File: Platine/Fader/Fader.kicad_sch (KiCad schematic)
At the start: 9 parts, among them J1 FaderPWR, J2 FaderSignal, J3 Motor13Out, J4 Motor4Out, J5 Conn_01x19, J6 Conn_01x19, U1 MC12, U3 MC34, U4 YAAJ_DCDC_StepDown_LM2596

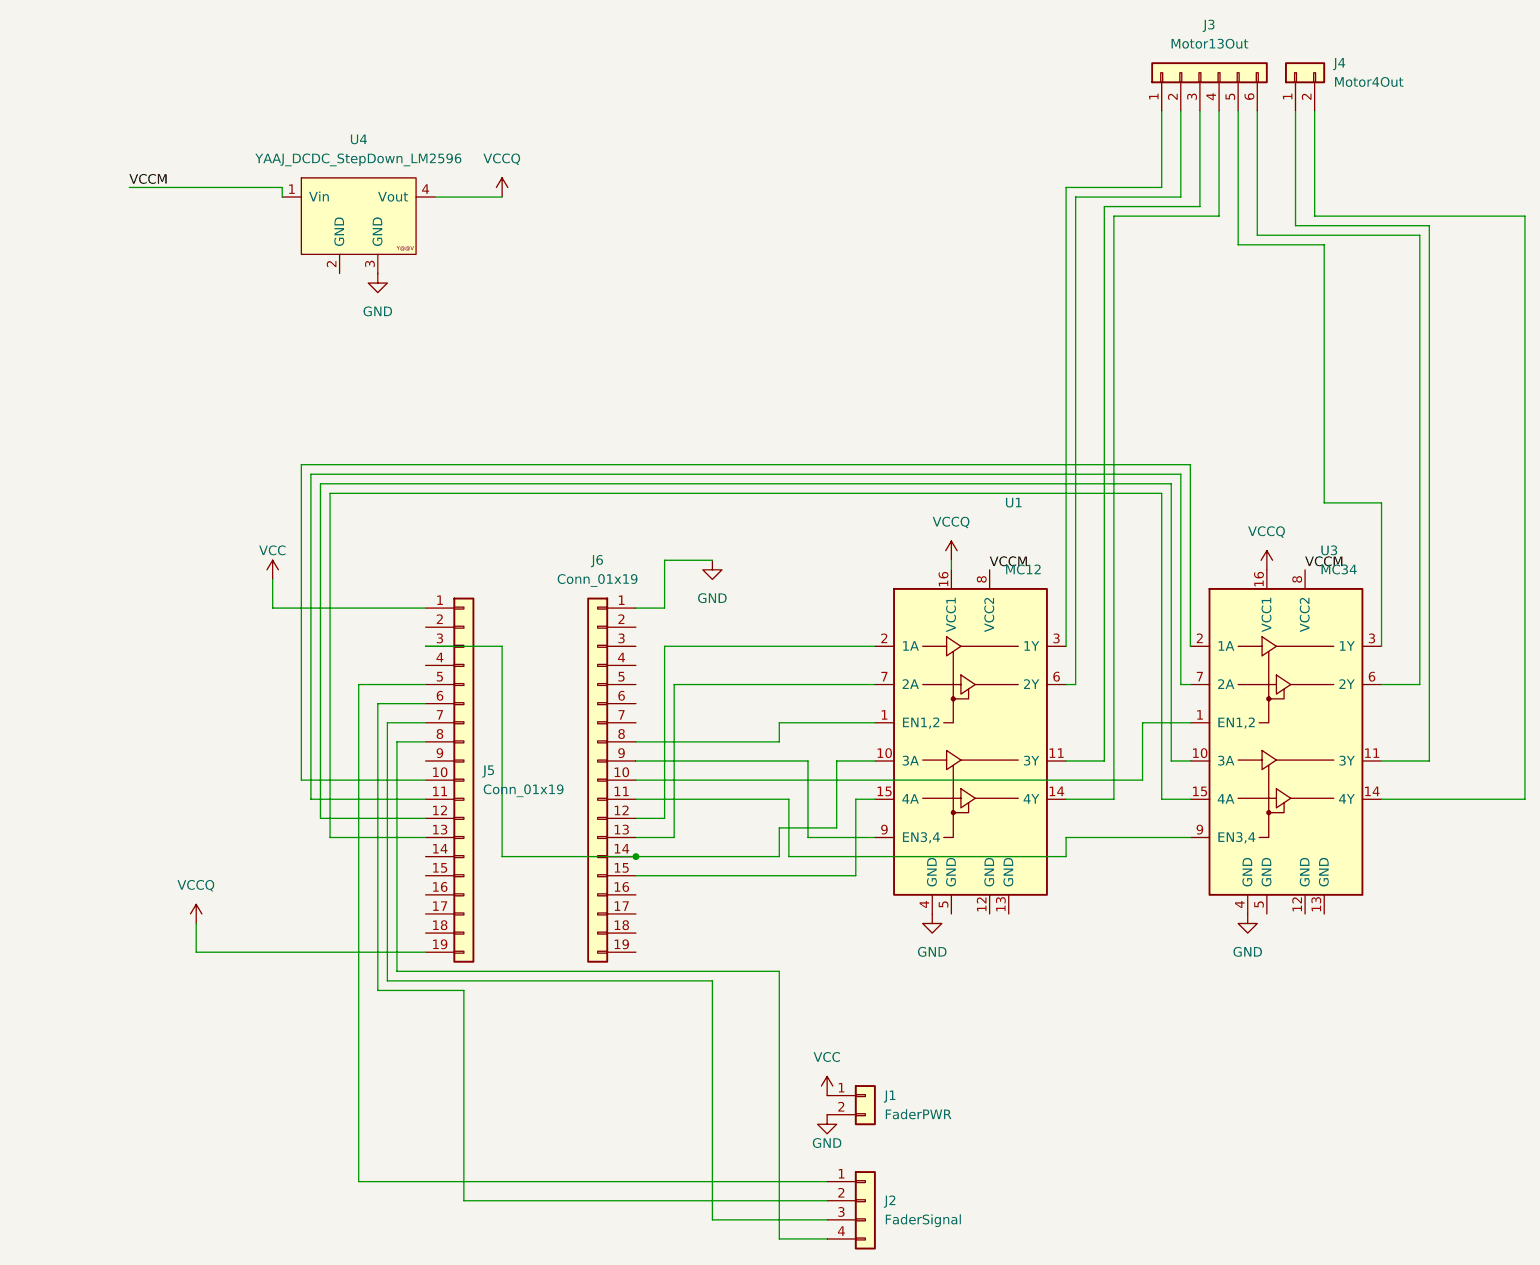
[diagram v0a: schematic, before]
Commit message: Rearranged pcb schematic. Added first traces and coorect ESP32 footprint model
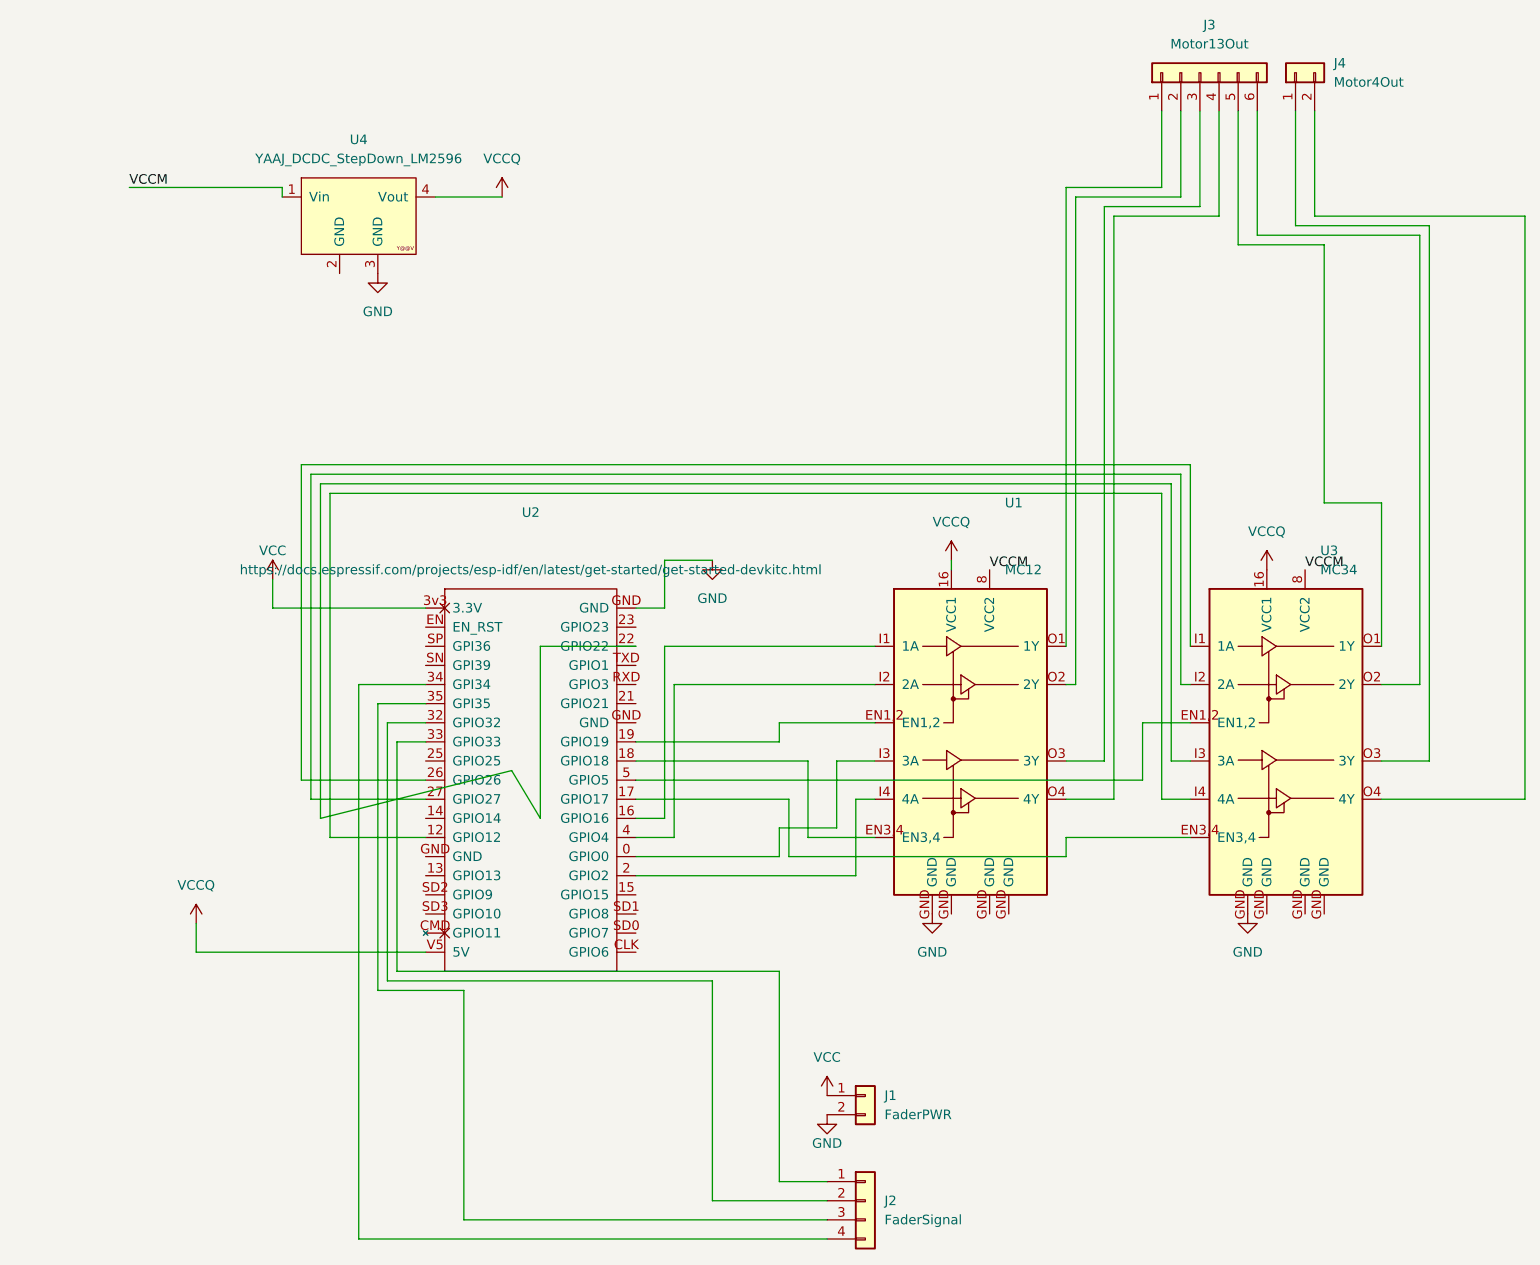
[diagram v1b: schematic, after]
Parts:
- removed J5: Conn_01x19, fp_esp32_dev4:esp32_dev_left, symbol Connector_Generic:Conn_01x19
- removed J6: Conn_01x19, fp_esp32_dev4:esp32_dev4_right, symbol Connector_Generic:Conn_01x19
- added U2: (no value), symbol New_Library:esp32_38_pins-custom_library
- U1, U3: symbol Driver_Motor:L293D -> New_Library:L293D
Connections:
- net GND: now also U1.GND, U3.GND, U2.GND; no longer U1.4 (GND), U3.4 (GND)
- net VCC: now also U2.3v3 (3.3V)
- net VCCQ: now also U2.V5 (5V)
- net at J3.1 (Pin_1): now also U1.O1 (1Y); no longer U1.3 (1Y)
- net at J3.2 (Pin_2): now also U1.O2 (2Y); no longer U1.6 (2Y)
- net at J3.3 (Pin_3): now also U1.O3 (3Y); no longer U1.11 (3Y)
- net at J3.4 (Pin_4): now also U1.O4 (4Y); no longer U1.14 (4Y)
- net at J3.5 (Pin_5): now also U3.O1 (1Y); no longer U3.3 (1Y)
- net at J3.6 (Pin_6): now also U3.O2 (2Y); no longer U3.6 (2Y)
- net at J4.1 (Pin_1): now also U3.O3 (3Y); no longer U3.11 (3Y)
- net at J4.2 (Pin_2): now also U3.O4 (4Y); no longer U3.14 (4Y)
- net at J2.1 (Pin_1): now also U2.33 (GPIO33)
- net at J2.2 (Pin_2): now also U2.32 (GPIO32)
- net at J2.3 (Pin_3): now also U2.35 (GPI35)
- net at J2.4 (Pin_4): now also U2.34 (GPI34)
- new net: U1.I3 (3A), U2.0 (GPIO0)
- new net: U2.12 (GPIO12), U3.I4 (4A)
- new net: U1.I1 (1A), U2.16 (GPIO16)
- new net: U2.17 (GPIO17), U3.EN3,4
- new net: U1.EN3,4, U2.18 (GPIO18)
- new net: U1.EN1,2, U2.19 (GPIO19)
- new net: U1.I4 (4A), U2.2 (GPIO2)
- new net: U2.22 (GPIO22), U3.I3 (3A)
- new net: U2.26 (GPIO26), U3.I1 (1A)
- new net: U2.27 (GPIO27), U3.I2 (2A)
- new net: U1.I2 (2A), U2.4 (GPIO4)
- new net: U2.5 (GPIO5), U3.EN1,2
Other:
- moved on the sheet: U1, U3

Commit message: Connect Slider Touch Pins to ESP32 touch sensitive pins
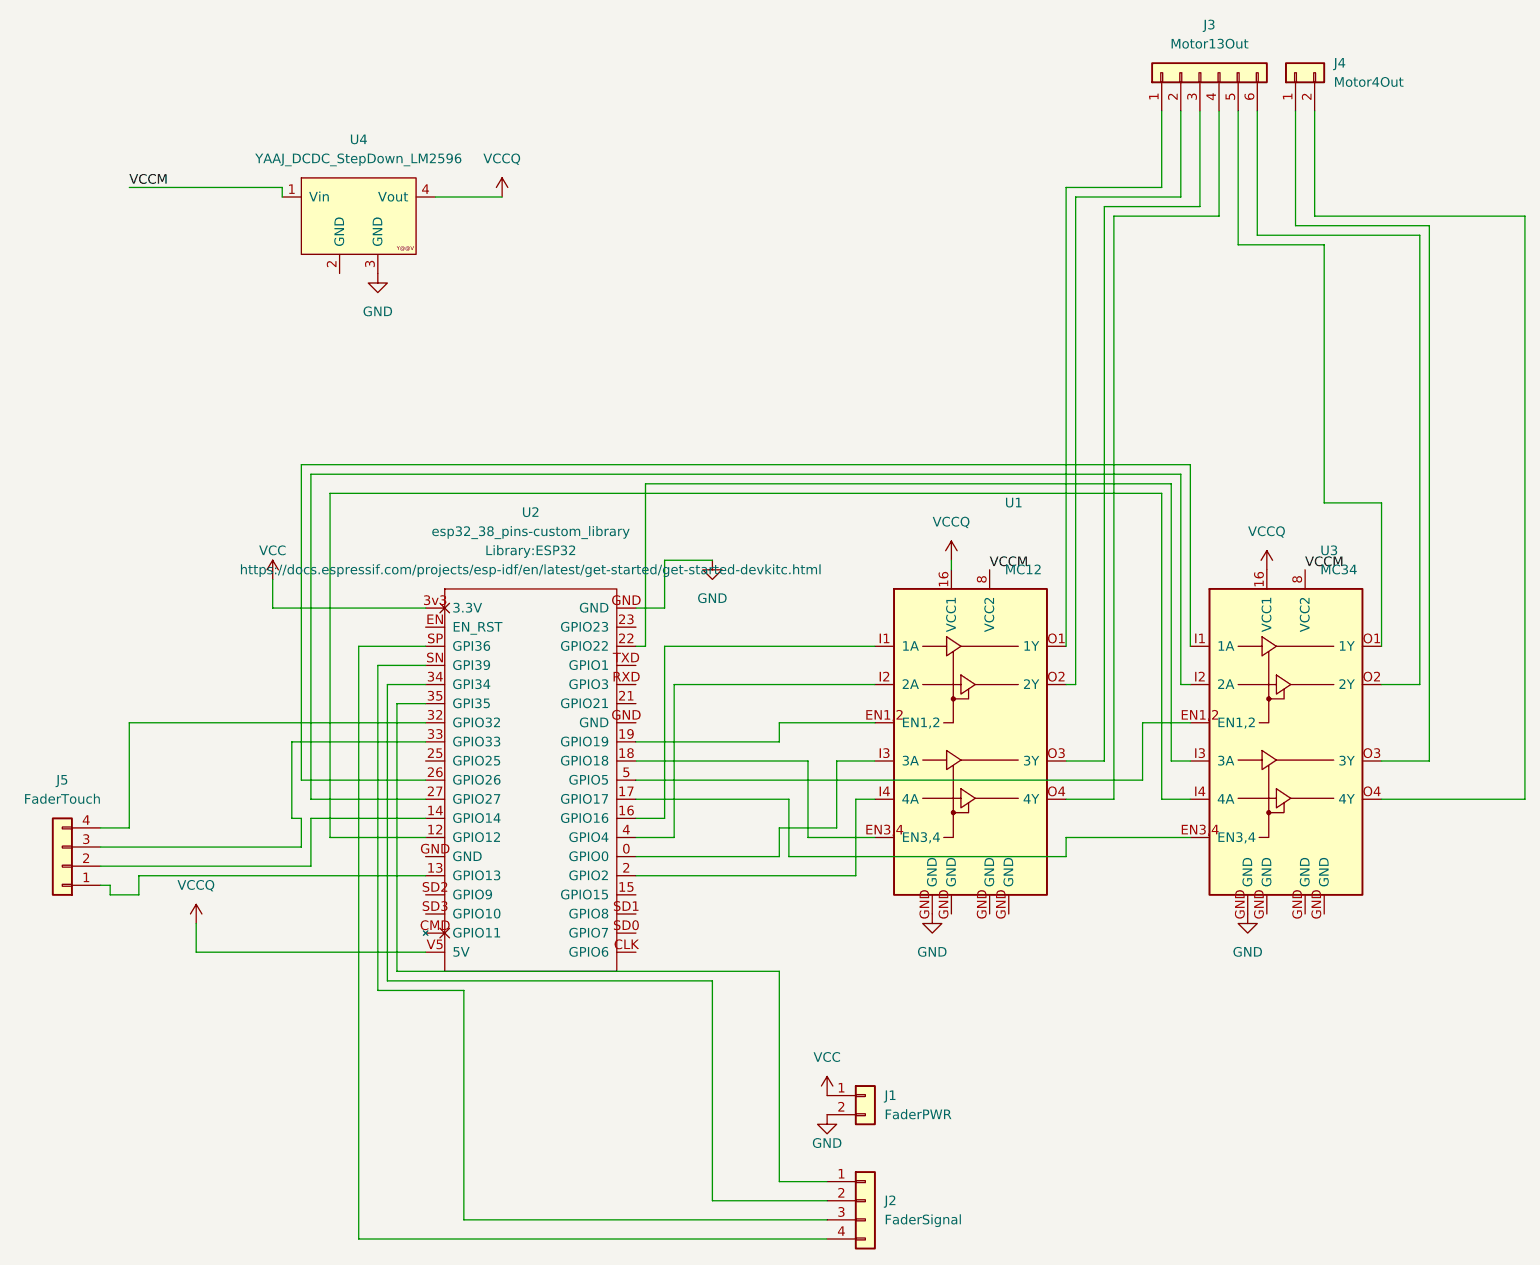
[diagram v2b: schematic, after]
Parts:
- added J5: FaderTouch, Connector_PinHeader_2.54mm:PinHeader_1x04_P2.54mm_Vertical, symbol Connector_Generic:Conn_01x04
- U2: value (none) -> esp32_38_pins-custom_library; footprint (none) -> Library:ESP32
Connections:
- net at U2.13 (GPIO13): now also J5.1 (Pin_1)
- net at U2.14 (GPIO14): now also J5.2 (Pin_2)
- net at U2.32 (GPIO32): now also J5.4 (Pin_4); no longer J2.2 (Pin_2)
- net at U2.33 (GPIO33): now also J5.3 (Pin_3); no longer J2.1 (Pin_1)
- net at U2.34 (GPI34): now also J2.2 (Pin_2); no longer J2.4 (Pin_4)
- net at U2.35 (GPI35): now also J2.1 (Pin_1); no longer J2.3 (Pin_3)
- net at U2.SN (GPI39): now also J2.3 (Pin_3)
- net at U2.SP (GPI36): now also J2.4 (Pin_4)
